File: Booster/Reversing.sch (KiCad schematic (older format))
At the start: 21 parts, among them J701 Conn_01x04, P701 REVERSER_OUT, P702 REVERSER_OUT_OP, Q701 BC817-40, SW601 DIP, U203 LM339, U701 74HC86, U702 PC817

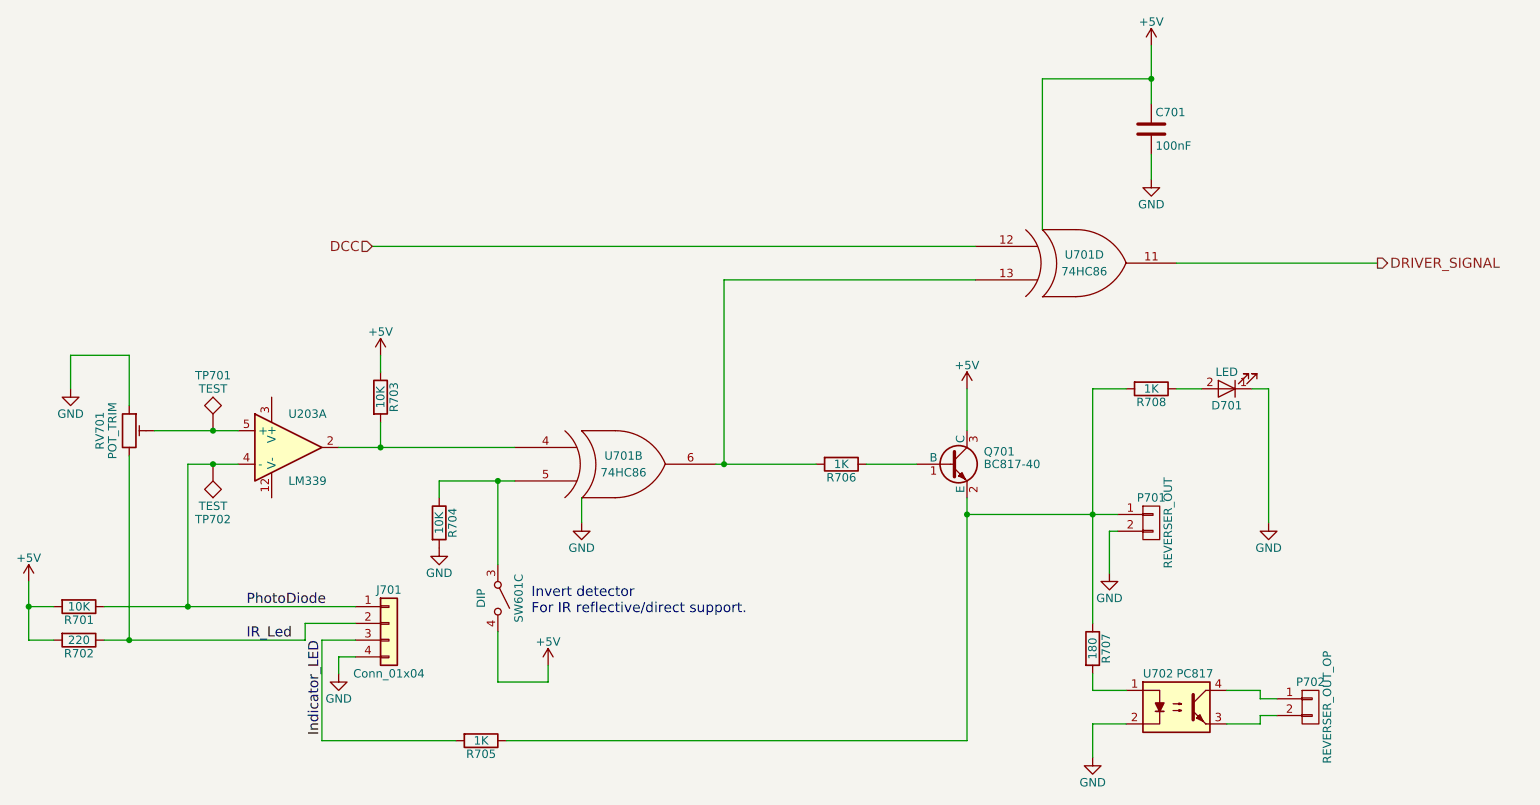
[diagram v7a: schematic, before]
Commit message: Increased resistor sizes on opt couplers and LED's to ensure the 78L05 can deliver enough power.
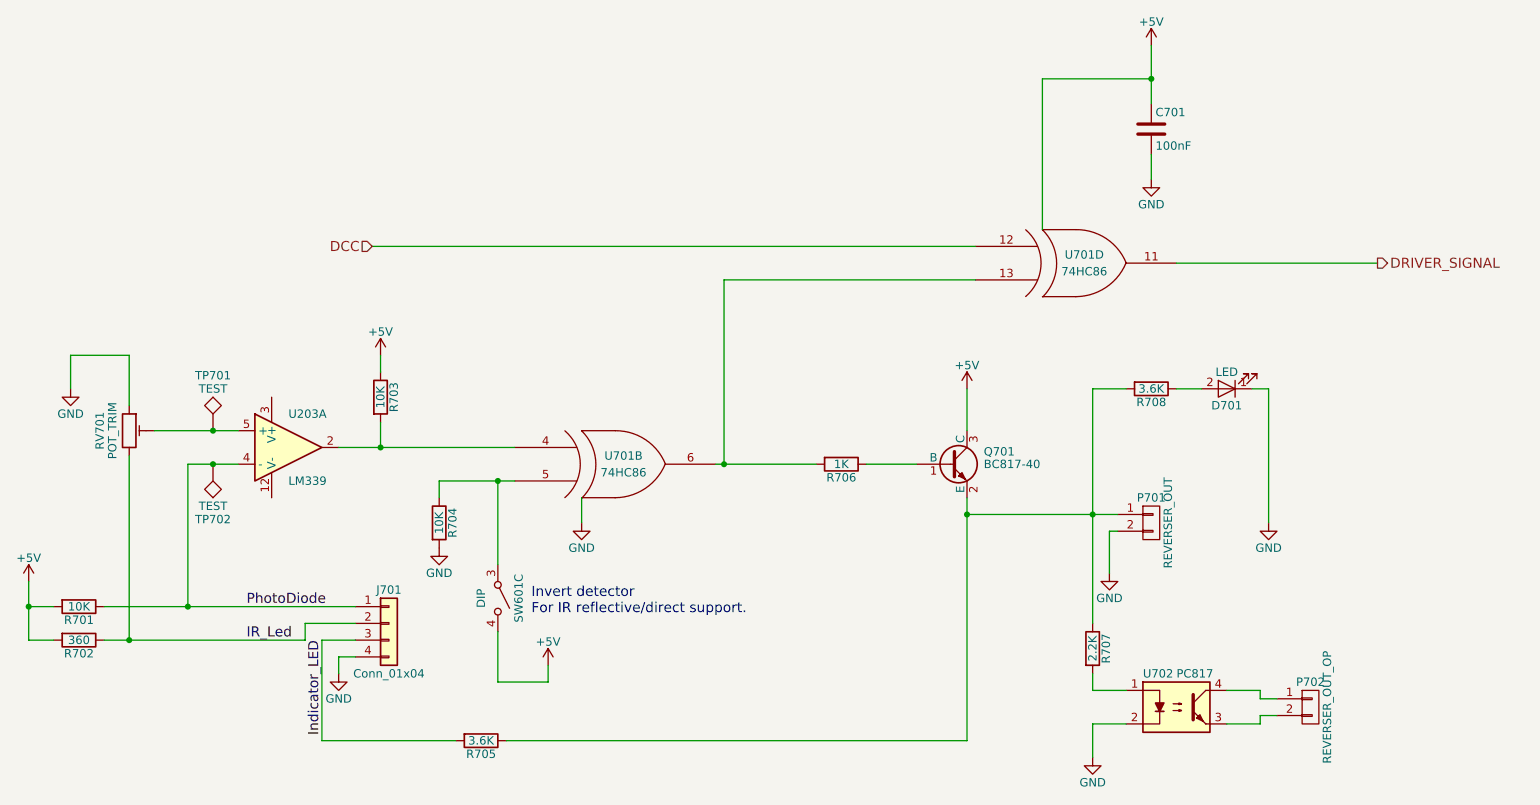
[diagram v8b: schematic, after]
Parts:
- R702: value 220 -> 360
- R705, R708: value 1K -> 3.6K
- R707: value 180 -> 2.2K
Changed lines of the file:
@@
 P 8650 3000
 F 0 "R708" V 8730 3000 50  0000 C CNN
-F 1 "1K" V 8650 3000 50  0000 C CNN
+F 1 "3.6K" V 8650 3000 50  0000 C CNN
 F 2 "Resistors_SMD:R_0805" V 8580 3000 50  0001 C CNN
 F 3 "" H 8650 3000 50  0000 C CNN
@@
 P 8300 4550
 F 0 "R707" V 8380 4550 50  0000 C CNN
-F 1 "180" V 8300 4550 50  0000 C CNN
+F 1 "2.2K" V 8300 4550 50  0000 C CNN
 F 2 "Resistors_SMD:R_0805" V 8230 4550 50  0001 C CNN
 F 3 "" H 8300 4550 50  0001 C CNN
@@
 P 2250 4500
 F 0 "R702" V 2330 4500 50  0000 C CNN
-F 1 "220" V 2250 4500 50  0000 C CNN
+F 1 "360" V 2250 4500 50  0000 C CNN
 F 2 "Resistors_SMD:R_0805" V 2180 4500 50  0001 C CNN
 F 3 "" H 2250 4500 50  0000 C CNN
@@
 P 4650 5100
 F 0 "R705" V 4730 5100 50  0000 C CNN
-F 1 "1K" V 4650 5100 50  0000 C CNN
+F 1 "3.6K" V 4650 5100 50  0000 C CNN
 F 2 "Resistors_SMD:R_0805" V 4580 5100 50  0001 C CNN
 F 3 "" H 4650 5100 50  0001 C CNN
